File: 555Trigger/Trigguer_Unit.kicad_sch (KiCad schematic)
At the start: 8 parts, among them U1 L272, U2 TLC555xP

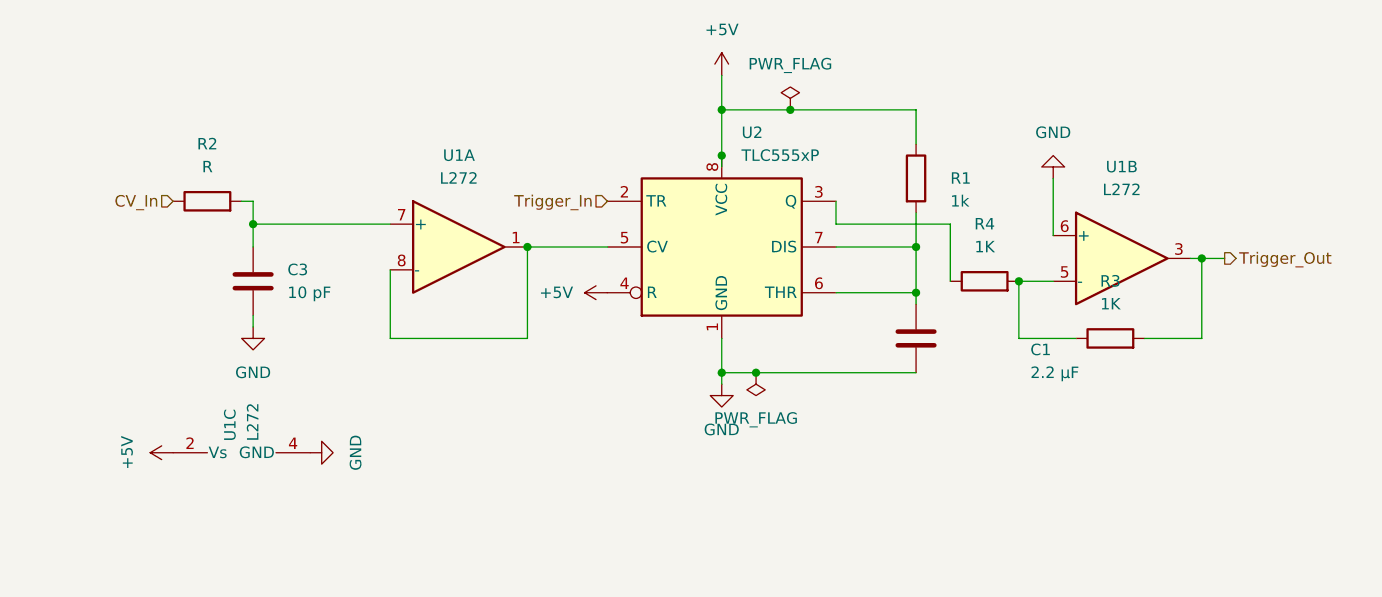
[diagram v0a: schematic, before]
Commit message: changed to SMD
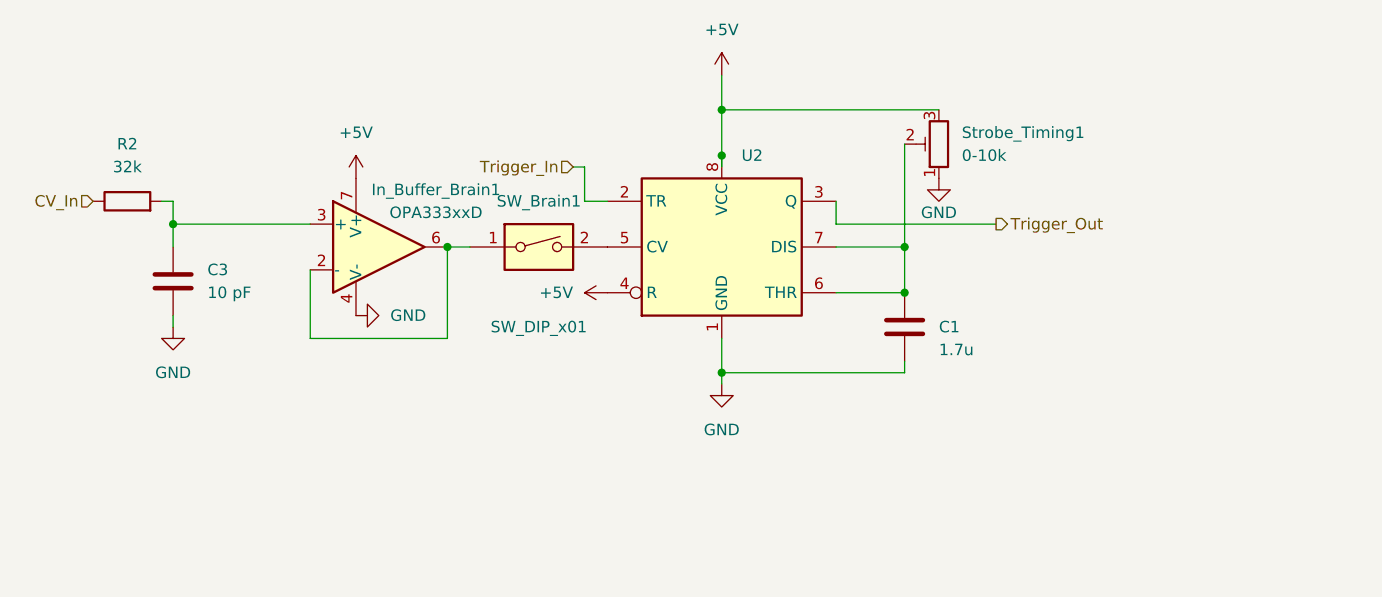
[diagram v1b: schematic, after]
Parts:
- removed R1: 1k, Resistor_THT:R_Axial_DIN0204_L3.6mm_D1.6mm_P5.08mm_Horizontal, symbol Device:R
- removed R3, R4: 1K, Resistor_THT:R_Axial_DIN0204_L3.6mm_D1.6mm_P5.08mm_Horizontal, symbol Device:R
- removed U1: L272, Package_DIP:DIP-16_W7.62mm, symbol Amplifier_Operational:L272
- added In_Buffer_Brain1: OPA333xxD, Package_SO:SOIC-8_3.9x4.9mm_P1.27mm, symbol Amplifier_Operational:OPA333xxD
- added SW_Brain1: SW_DIP_x01, Button_Switch_SMD:SW_DIP_SPSTx01_Slide_9.78x4.72mm_W8.61mm_P2.54mm, symbol Switch:SW_DIP_x01
- added Strobe_Timing1: 0-10k, Potentiometer_SMD:Potentiometer_ACP_CA14-VSMD_Vertical_Hole, symbol Device:R_Potentiometer_Trim
- C1: value 2.2 μF -> 1.7u; footprint Capacitor_THT:CP_Axial_L10.0mm_D4.5mm_P15.00mm_Horizontal -> Capacitor_SMD:C_1206_3216Metric_Pad1.33x1.80mm_HandSolder
- C3: footprint Capacitor_THT:CP_Axial_L10.0mm_D4.5mm_P15.00mm_Horizontal -> Capacitor_SMD:C_0603_1608Metric_Pad1.08x0.95mm_HandSolder
- R2: value R -> 32k; footprint Resistor_THT:R_Axial_DIN0204_L3.6mm_D1.6mm_P5.08mm_Horizontal -> Resistor_SMD:R_0805_2012Metric_Pad1.20x1.40mm_HandSolder
- U2: value TLC555xP -> TLC555xD; footprint Package_DIP:DIP-8_W7.62mm -> Package_SO:SOIC-8_3.9x4.9mm_P1.27mm; symbol Timer:TLC555xP -> Timer:TLC555xD
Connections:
- net +5V: now also In_Buffer_Brain1.7 (V+), Strobe_Timing1.3
- net GND: now also In_Buffer_Brain1.4 (V-), Strobe_Timing1.1
- net Trigger_Out: now also U2.3 (Q)
- net at U2.5 (CV): now also SW_Brain1.2
- net at C3.1, R2.2: now also In_Buffer_Brain1.3 (+)
- net at C1.1, U2.6 (THR), U2.7 (DIS): now also Strobe_Timing1.2
- new net: In_Buffer_Brain1.2 (-), In_Buffer_Brain1.6, SW_Brain1.1
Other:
- moved on the sheet: C1, C3, R2

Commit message: updated timer design
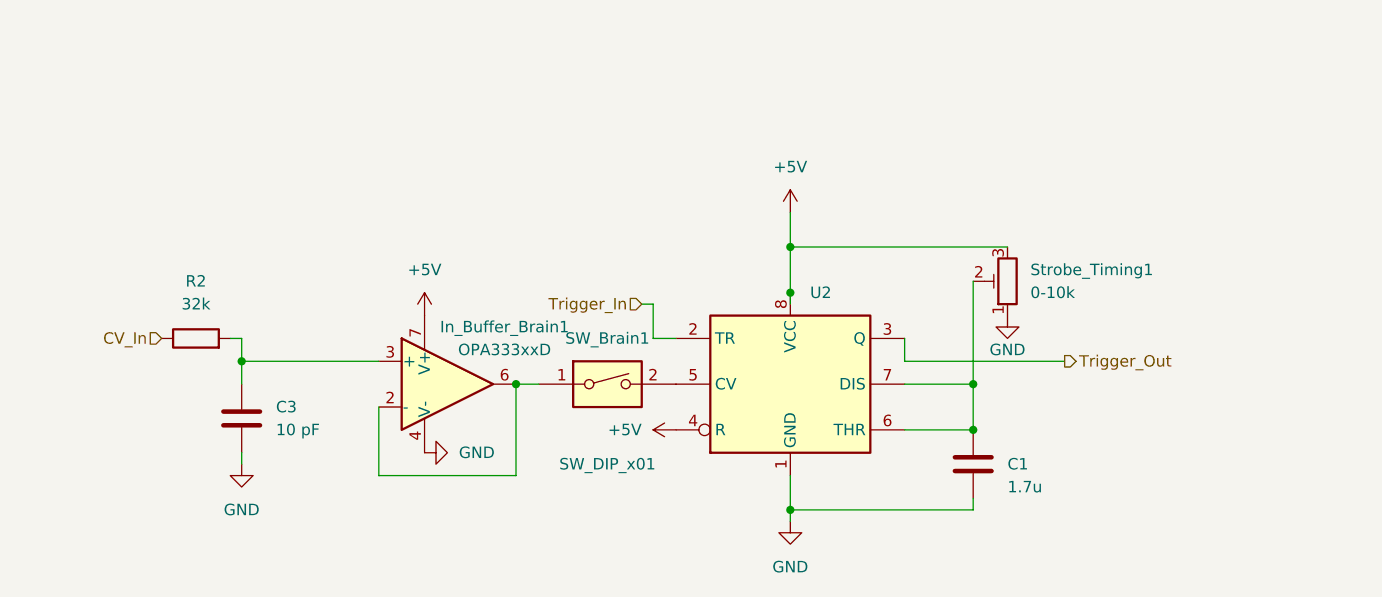
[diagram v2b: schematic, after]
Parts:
- Strobe_Timing1: footprint Potentiometer_SMD:Potentiometer_ACP_CA14-VSMD_Vertical_Hole -> Potentiometer_SMD:Potentiometer_ACP_CA9-VSMD_Vertical
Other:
- moved on the sheet: C1, C3, In_Buffer_Brain1, R2, SW_Brain1, Strobe_Timing1, U2

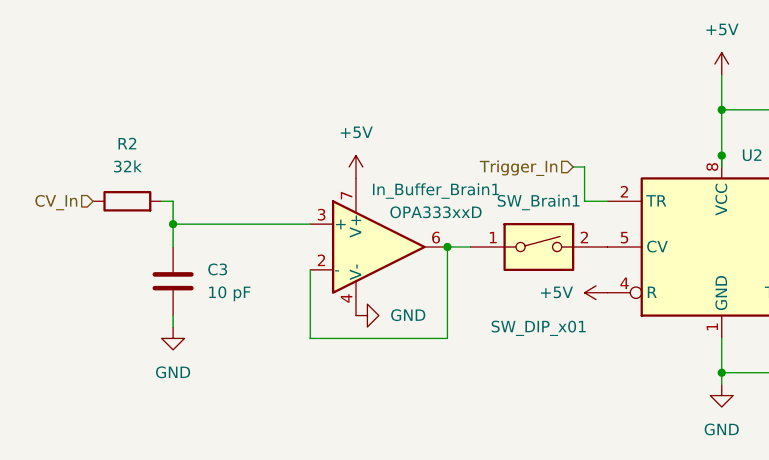
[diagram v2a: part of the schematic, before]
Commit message: changed some components to make manufacturing simpler
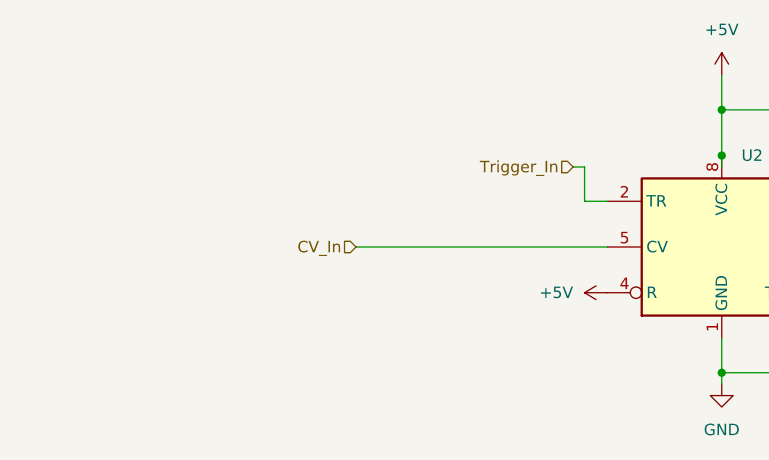
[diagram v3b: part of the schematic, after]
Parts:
- removed C3: 10 pF, Capacitor_SMD:C_0603_1608Metric_Pad1.08x0.95mm_HandSolder, symbol Device:C
- removed In_Buffer_Brain1: OPA333xxD, Package_SO:SOIC-8_3.9x4.9mm_P1.27mm, symbol Amplifier_Operational:OPA333xxD
- removed R2: 32k, Resistor_SMD:R_0805_2012Metric_Pad1.20x1.40mm_HandSolder, symbol Device:R
- removed SW_Brain1: SW_DIP_x01, Button_Switch_SMD:SW_DIP_SPSTx01_Slide_9.78x4.72mm_W8.61mm_P2.54mm, symbol Switch:SW_DIP_x01
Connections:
- net CV_In: now also U2.5 (CV)

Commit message: changed components to be easier to order
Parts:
- C1: value 1.7u -> 2.2uF; footprint Capacitor_SMD:C_1206_3216Metric_Pad1.33x1.80mm_HandSolder -> Capacitor_SMD:C_0805_2012Metric
- Strobe_Timing1: footprint Potentiometer_SMD:Potentiometer_ACP_CA9-VSMD_Vertical -> Potentiometer_SMD:Potentiometer_Bourns_3314J_Vertical
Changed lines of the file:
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@@
       (effects (font (size 1.27 1.27)) (justify right))
     )
-    (property "Footprint" "Potentiometer_SMD:Potentiometer_ACP_CA9-VSMD_Vertical" (at 185.42 83.82 0)
+    (property "Footprint" "Potentiometer_SMD:Potentiometer_Bourns_3314J_Vertical" (at 185.42 83.82 0)
       (effects (font (size 1.27 1.27)) hide)
     )
@@
       (effects (font (size 1.27 1.27)) (justify left))
     )
-    (property "Value" "1.7u" (at 185.42 106.68 0)
-      (effects (font (size 1.27 1.27)) (justify left))
-    )
-    (property "Footprint" "Capacitor_SMD:C_1206_3216Metric_Pad1.33x1.80mm_HandSolder" (at 182.5752 107.95 0)
-      (effects (font (size 1.27 1.27)) hide)
-    )
+    (property "Value" "2.2uF" (at 185.42 106.68 0)
+      (effects (font (size 1.27 1.27)) (justify left))
+    )
+    (property "Footprint" "Capacitor_SMD:C_0805_2012Metric" (at 182.5752 107.95 0)
+      (effects (font (size 1.27 1.27)) hide)
+    )
